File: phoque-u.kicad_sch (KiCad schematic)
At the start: 60 parts, among them J1 18…56 V, J2 On / Off, J3 3.3…24 V, Q1 SiR120DP, Q2 SiR120DP, Q3 SiR120DP, Q4 SiR120DP, SW1 Remote, SW2 Voltage select, T1 320 µ, T2 180 µ, U1 LT4320, U2 i7A4W033A033V

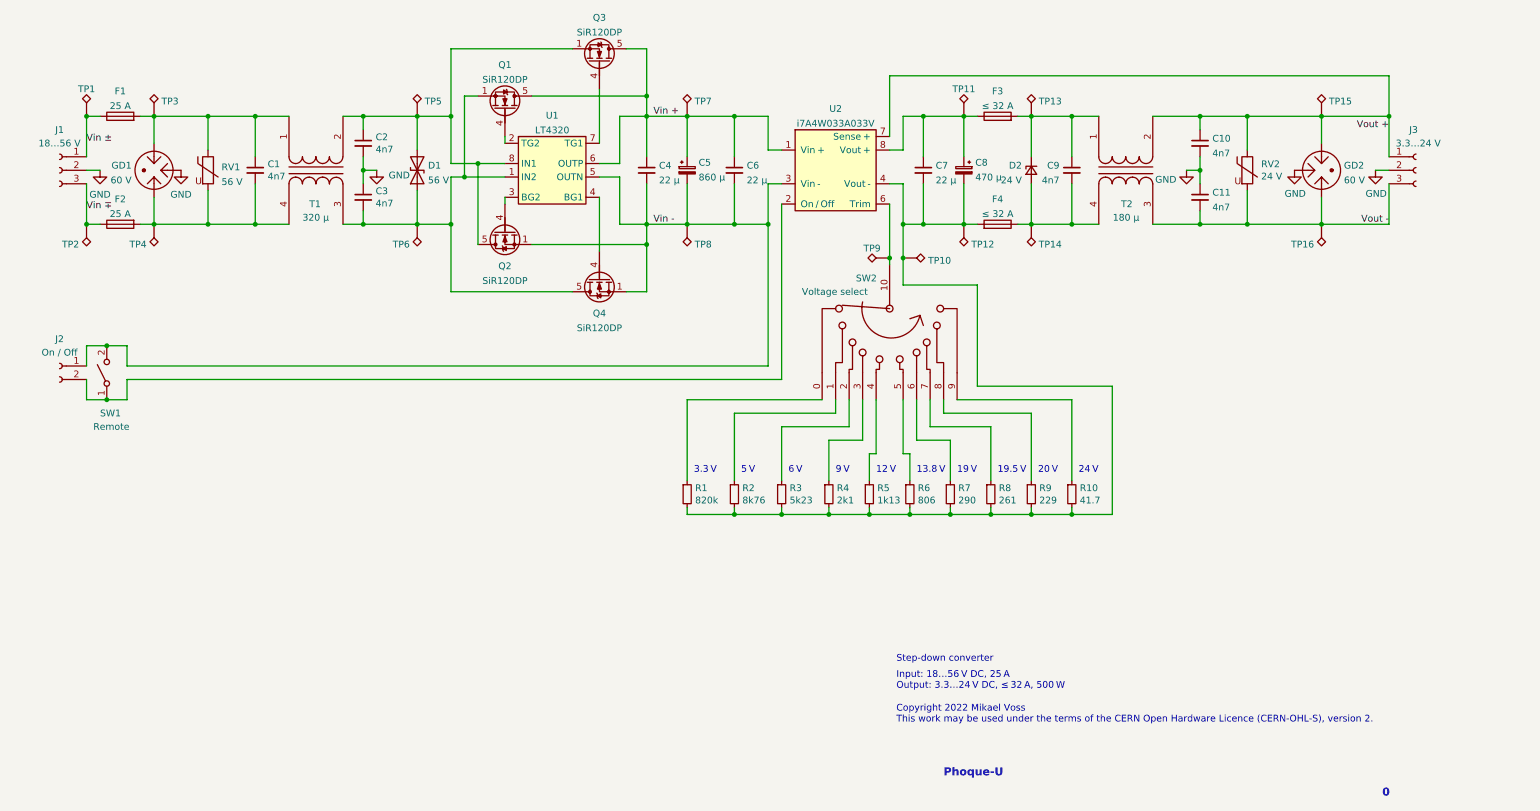
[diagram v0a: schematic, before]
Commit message: Update schematic according to parts availability
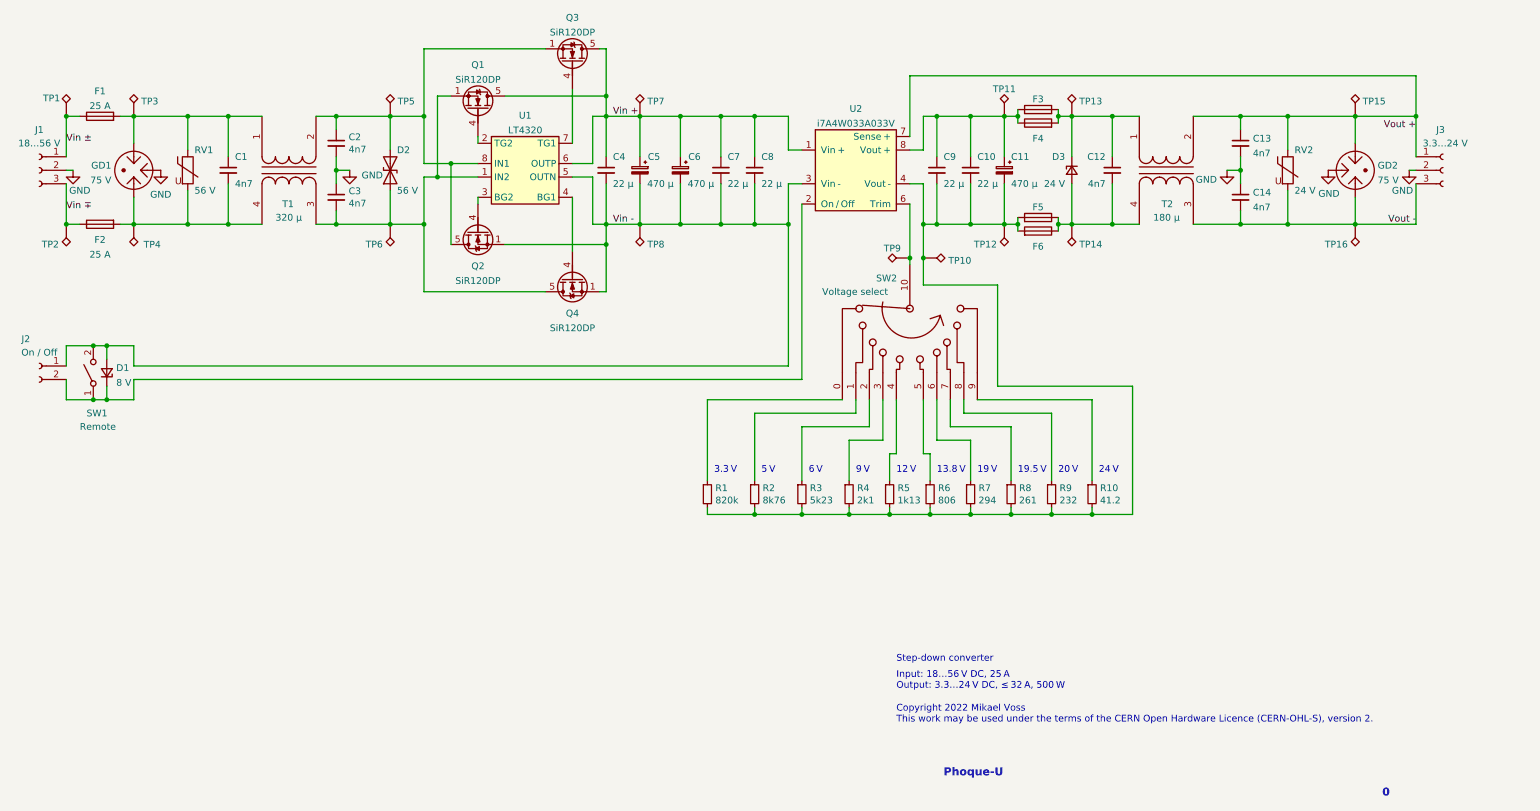
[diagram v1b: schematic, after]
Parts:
- added C10, C7: 22 µ, symbol Device:C_Small
- added C6: 470 µ, Capacitor_THT:CP_Radial_D16.0mm_P7.50mm, symbol Device:C_Polarized_Small
- added D1: 8 V, symbol Device:D_Zener_Small
- added F4, F6: ≤ 32 A, symbol Device:Fuse
- C11: renamed from C8; footprint Capacitor_THT:CP_Radial_D18.0mm_P7.50mm -> Capacitor_THT:CP_Radial_D16.0mm_P7.50mm; Part Number UHE2A471MHD6 -> URZ1J471MHD
- C4: Part Number C5750X7S2A226M280KB -> KRM55WR71J226MH01K
- C5: value 860 µ -> 470 µ; footprint Capacitor_THT:CP_Radial_D18.0mm_P7.50mm -> Capacitor_THT:CP_Radial_D16.0mm_P7.50mm; Part Number UHE1J821MHD6 -> URZ1J471MHD
- C8: renamed from C6; Part Number C5750X7S2A226M280KB -> KRM55WR71J226MH01K
- C9: renamed from C7; Part Number C5750X7S2A226M280KB -> KRM55WR71J226MH01K
- D3: renamed from D2; footprint (none) -> Diode_SMD:D_SMC
- F1, F3: Part Number (none) -> 3557
- F5: renamed from F4; Part Number (none) -> 3557
- GD1, GD2: value 60 V -> 75 V; Part Number 2020-15T-C2FLF -> 2036-07-SM
- Q2: Part Number (none) -> SiR120DP
- R10: value 41.7 -> 41.2
- R7: value 290 -> 294
- R9: value 229 -> 232
- renumbered C9 to C12, C10 to C13, C11 to C14, D1 to D2
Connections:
- net Vin +: now also C6.1, C7.1
- net Vin -: now also C6.2, C7.2, D1.2 (A)
- net at C12.1, D3.1 (K), F3.2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: now also F4.2
- net at C12.2, D3.2 (A), F5.1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: now also F6.1
- net at C11.1, C9.1, F3.1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: now also C10.1, F4.1
- net at C11.2, C9.2, F5.2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: now also C10.2, F6.2
- net at J2.2 (Pin_2), SW1.1 (A), U2.2 (On / Off): now also D1.1 (K)
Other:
- moved on the sheet: C1, C11, C12, C13, C14, C2, C3, C4, C5, C8, C9, D2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

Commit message: Specify full part number for DC/DC module
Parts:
- U2: Part Number (none) -> i7A4W033A033V-0C1
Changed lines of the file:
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@@
+      (effects (font (size 1.27 1.27)) hide)
+    )
+    (property "Part Number" "i7A4W033A033V-0C1" (id 4) (at 170.18 76.2 0)
       (effects (font (size 1.27 1.27)) hide)
     )

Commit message: Add footprints
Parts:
- C10, C7: footprint (none) -> Local:C_Rect_L26.5mm_W12mm_P22.50mm_MKT
- C4, C8, C9: footprint (none) -> Local:KRM55WR71J226MH01
- D1: footprint (none) -> Diode_SMD:D_SMF
- F1, F2, F3, F5: footprint (none) -> Local:3557
- F4, F6: footprint (none) -> Local:8040
- GD1, GD2: footprint (none) -> Local:2036-NN-SM
- J1, J3: footprint (none) -> Local:2606-1103; Part Number (none) -> 2606-1103
- J2: footprint (none) -> Local:2604-1102; Part Number (none) -> 2604-1102
- R1, R10, R2, R3, R4, R5, R6, R7, R8, R9, RV1, RV2: footprint (none) -> Resistor_SMD:R_0805_2012Metric
- SW1: Part Number (none) -> 418127270901
- TP1, TP10, TP11, TP12, TP13, TP14, TP15, TP16, TP2, TP3, TP4, TP5, TP6, TP7, TP8, TP9: footprint (none) -> TestPoint:TestPoint_Pad_D1.5mm

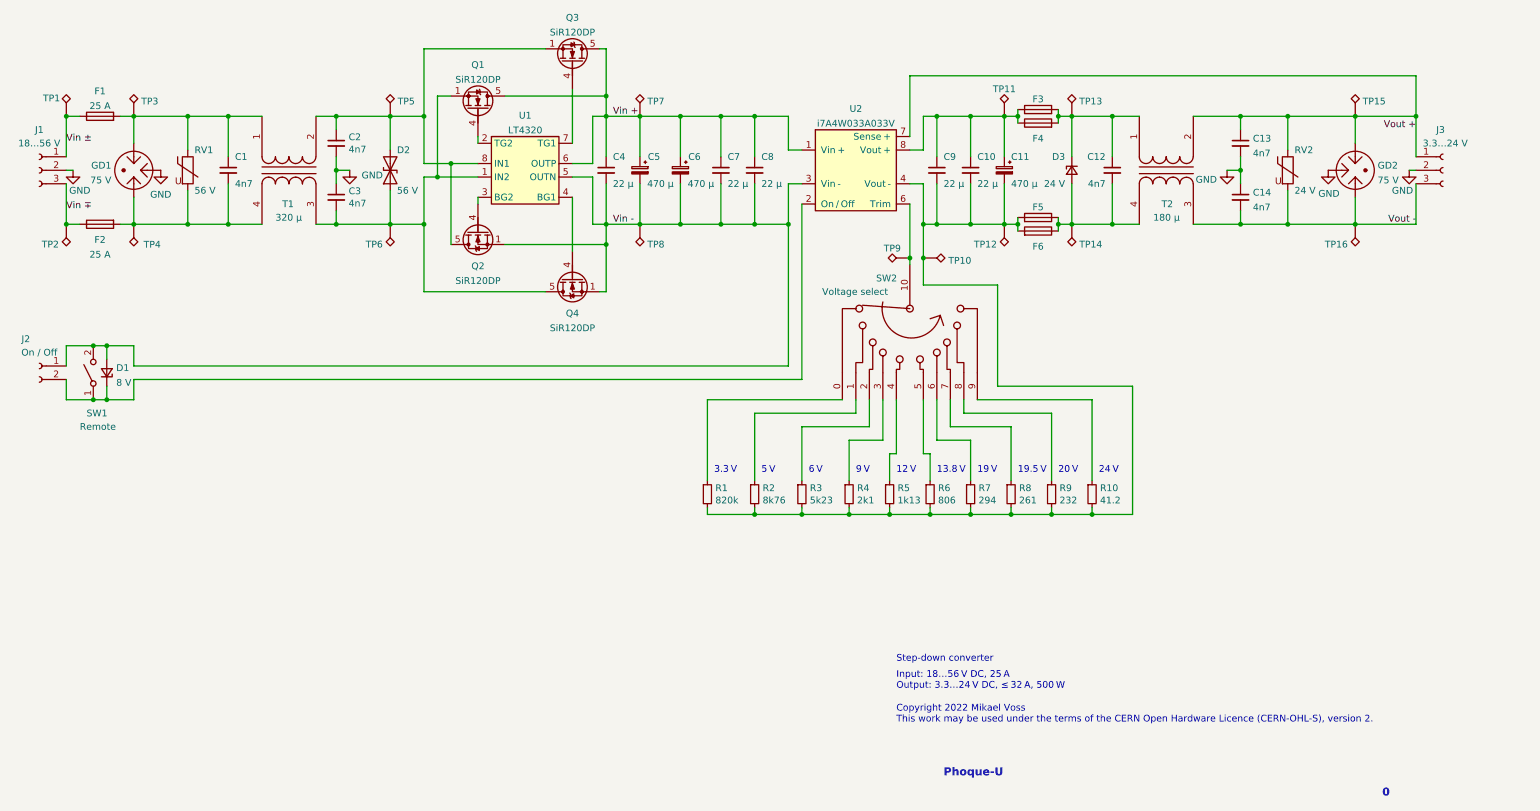
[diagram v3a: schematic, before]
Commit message: Replace switches
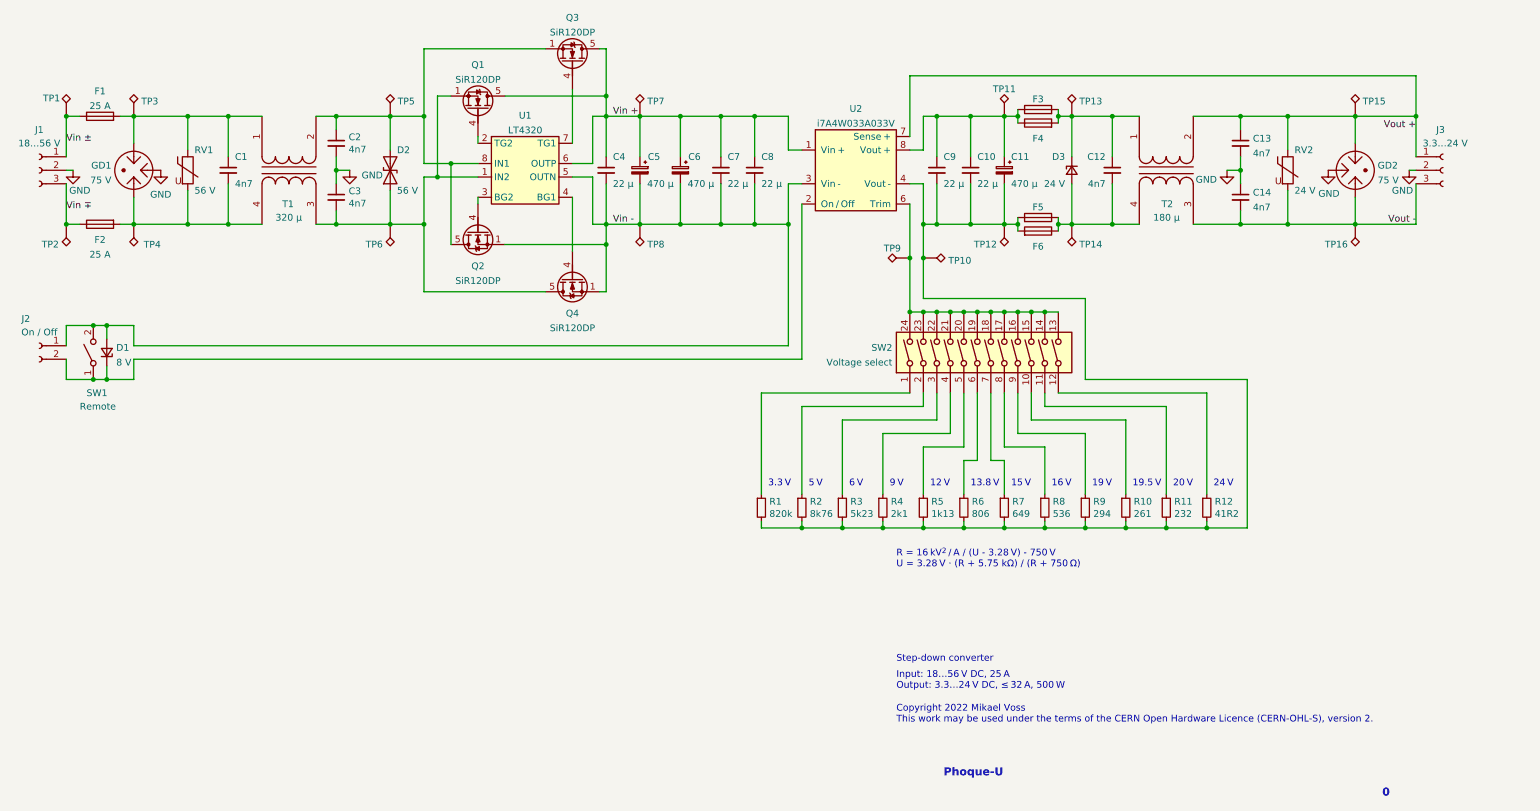
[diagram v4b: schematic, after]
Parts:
- removed SW2: Voltage select, symbol Local:SW_Rotary10
- added R7: 649, Resistor_SMD:R_0805_2012Metric, symbol Device:R_Small
- added R8: 536, Resistor_SMD:R_0805_2012Metric, symbol Device:R_Small
- added SW2: Voltage select, Local:418127160912, symbol Switch:SW_DIP_x12
- R12: renamed from R10; value 41.2 -> 41R2
- SW1: footprint (none) -> Local:418127160901; Manufacturer (none) -> Würth Elektronik; Part Number 418127270901 -> 418127160901
- T1: footprint (none) -> Local:CMX1211Z321B-10
- T2: footprint (none) -> Local:CMX1211Z181B-10
- U2: footprint Local:U_i7A4W033A033V -> Local:i7A4W033A033V-0C1
- renumbered R8 to R10, R9 to R11, R7 to R9
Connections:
- net at C10.2, C11.2, C9.2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: now also R7.2, R8.2
- net at TP9.1, U2.6 (Trim): now also SW2.13, SW2.14, SW2.15, SW2.16, SW2.17, SW2.18, SW2.19, SW2.20, SW2.21, SW2.22, SW2.23, SW2.24
- net at R1.1: now also SW2.1
- net at R2.1: now also SW2.2
- net at R3.1: now also SW2.3
- net at R4.1: now also SW2.4
- net at R5.1: now also SW2.5
- net at R6.1: now also SW2.6
- net at R9.1: now also SW2.9
- net at R10.1: now also SW2.10
- net at R11.1: now also SW2.11
- net at R12.1: now also SW2.12
- new net: R7.1, SW2.7
- new net: R8.1, SW2.8
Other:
- note added: "15 V"
- note added: "16 V"
- note added: "R = 16 kV^{2} / A / (U - 3.28 V) - 750 V U = 3.28 V · (R + 5.75 kΩ) / (R + 750 Ω)"
- moved on the sheet: D1, J2, R1, R10, R11, R12, R2, R3, R4, R5, R6, R9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

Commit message: i7A4W033A033V: Remove pins 9 & 10
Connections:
- net Vin +: no longer U2.9 (Vin +)
- net Vin -: no longer U2.10 (Vin -)
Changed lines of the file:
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@@
     )
     (pin "1")
-    (pin "10")
     (pin "2")
     (pin "3")
@@
     (pin "7")
     (pin "8")
-    (pin "9")
   )
   (symbol (lib_id "Connector:Conn_01x02_Female") (at 16.51 109.22 0) (mirror y) (unit 1)

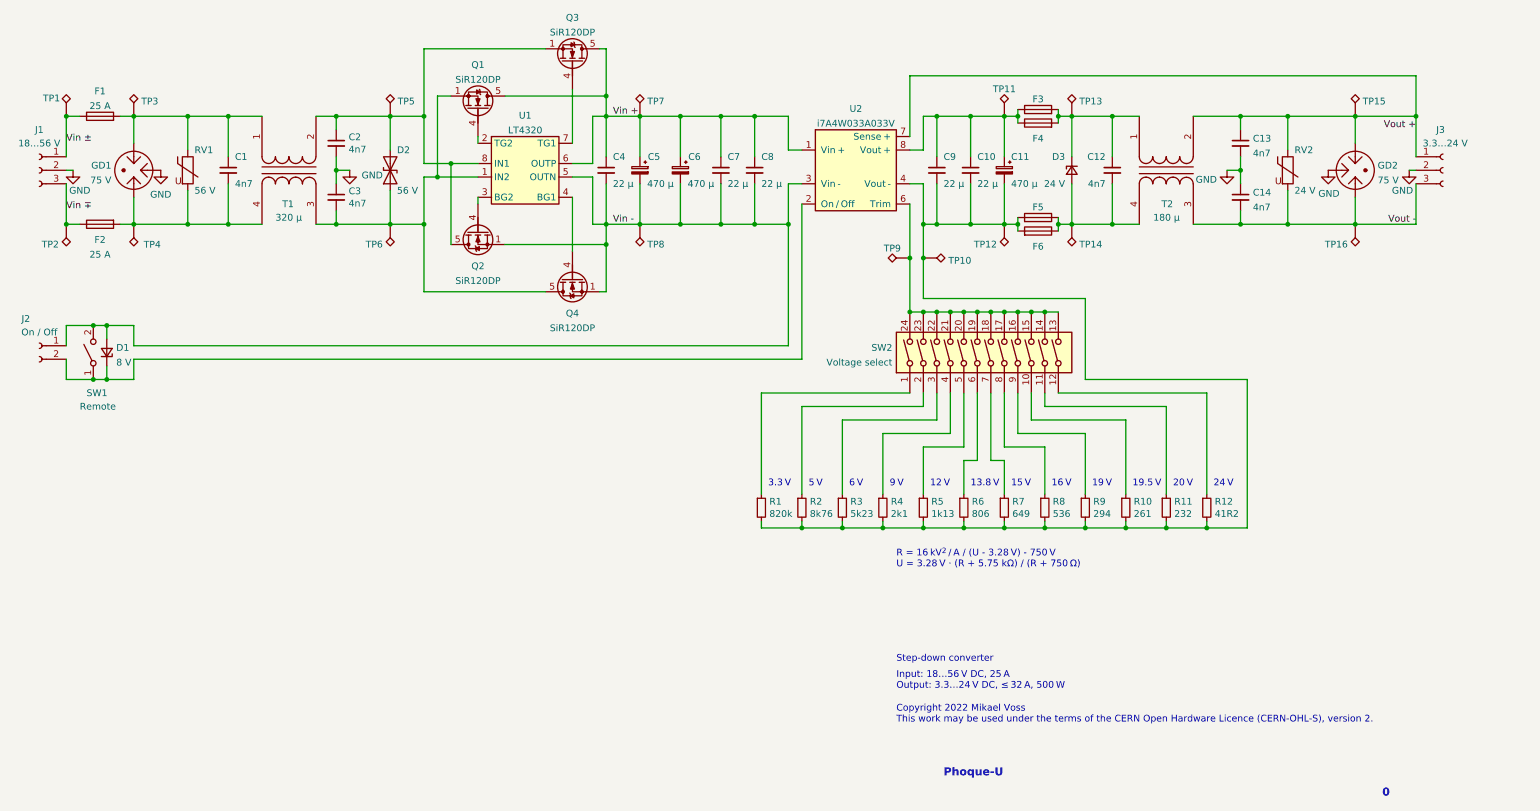
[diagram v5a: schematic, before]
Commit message: Remove film capacitors
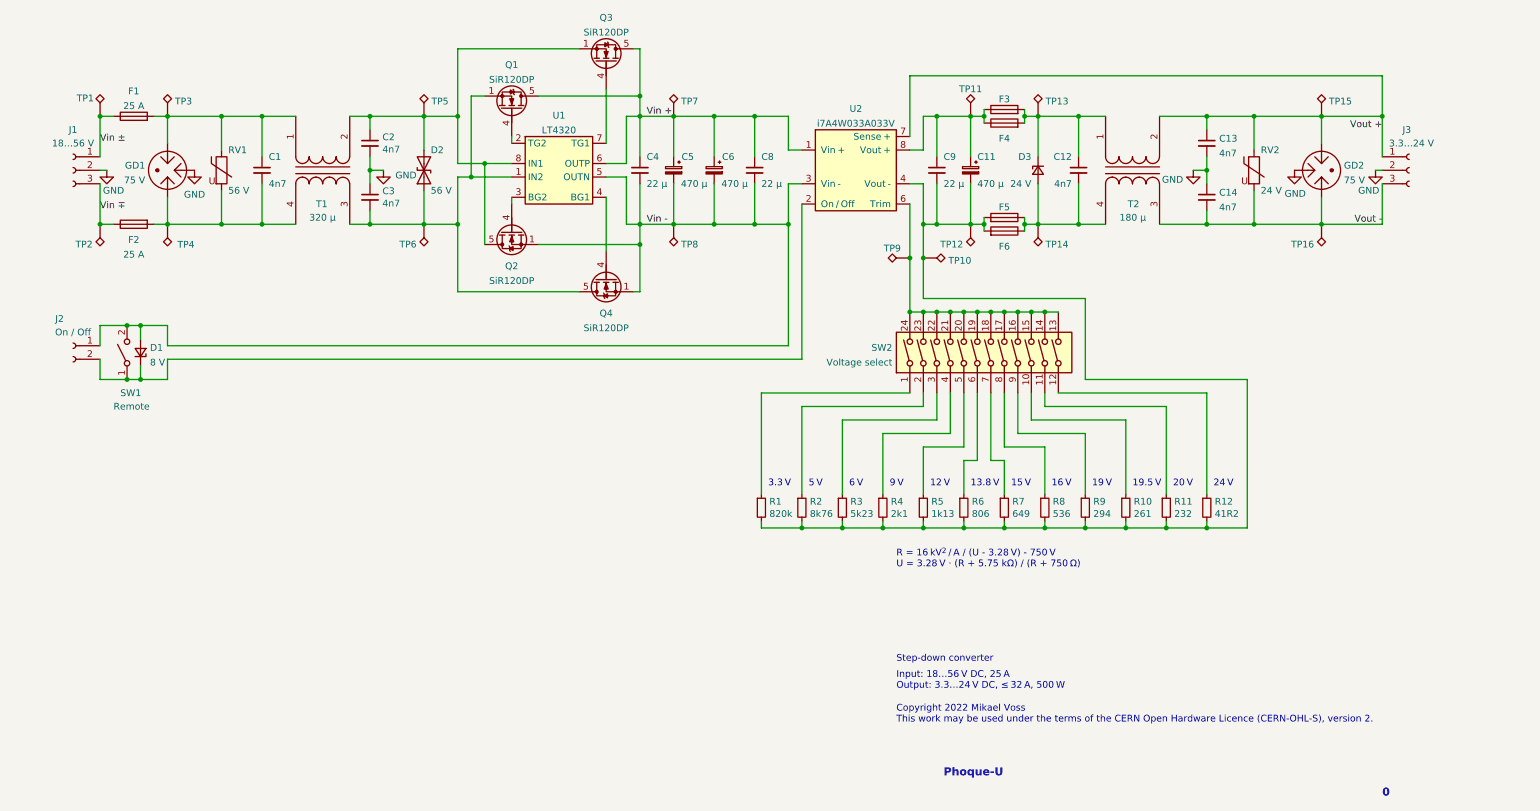
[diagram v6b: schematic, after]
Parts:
- removed C10, C7: 22 µ, Local:C_Rect_L26.5mm_W12mm_P22.50mm_MKT, symbol Device:C_Small
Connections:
- net Vin +: no longer Q1.6 (D), Q1.7 (D), Q1.8 (D), Q3.6 (D), Q3.7 (D), Q3.8 (D)
- net at C2.1, D2.2 (A2), Q2.5 (D)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: no longer Q2.6 (D), Q2.7 (D), Q2.8 (D)
- net at C3.2, D2.1 (A1), Q1.1 (S)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: no longer Q4.6 (D), Q4.7 (D), Q4.8 (D)
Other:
- moved on the sheet: C1, C11, C12, C13, C14, C2, C3, C4, C5, C6, D1, D2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
